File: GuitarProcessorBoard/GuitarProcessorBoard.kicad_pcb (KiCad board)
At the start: 4 copper layers, 141 parts, among them J301 SWD Header, J302 PWR, J303 TAP, J304 MODE, J305 BYP, J306 EXP, J307 ScopeGroundLoop, SW301 RST, SW302 BOOT, SW303 ENC, SW304 BACK, U201 TLV320AIC3204, U202 TL074, U301 STM32H7B0VBT6, U302 TPS63070, U304 74HC595, Y301 32MHz, Y302 32.768kHZ

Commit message: starting layout
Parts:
- removed C208, C213: 100n, Capacitor_SMD:C_0805_2012Metric
- added R220: 22, Resistor_SMD:R_0805_2012Metric, B.Cu at (-134.1, 76.3)
- added R330: 22, Resistor_SMD:R_0805_2012Metric, B.Cu at (-143.9, 74.0)
- added R331: 22, Resistor_SMD:R_0805_2012Metric, B.Cu at (-146.1, 76.3)
- added R332: 22, Resistor_SMD:R_0805_2012Metric, B.Cu at (-141.4, 71.7)
- added R333: 22, Resistor_SMD:R_0805_2012Metric, B.Cu at (-139.9, 70.2)
- C201, C202, C203, C204, C205, C206, C207, C209, C210, C211, C212, C214, C215, C216, C217, C218, C219, C303, C304, C305, C306, C307, C308, C309, C310, C311, C312, C313, C314, C315, C316, C317, C318, C327, C328, C329, C330, C331, C332, C333, C334, D303, D304, FB301, J301, J302, J303, J304, J305, J306, J307, R201, R202, R203, R204, R205, R206, R207, R208, R209, R210, R211, R212, R213, R214, R215, R216, R217, R218, R219, R301, R302, R303, R304, R305, R306, R307, R308, R309, R310, R315, R316, R317, R318, R319, R320, R321, R322, R323, R324, R325, R326, R327, R328, R329, SW301, SW302, TP201, TP202, TP203, TP301, TP302, TP303, U201, U202, U301, U304, Y301, Y302: moved to B.Cu
- C301, C302: value 6p -> 10p; moved to B.Cu
- RV201, RV301, RV302, RV303: footprint Potentiometer_THT:Potentiometer_Alpha_RV16AF_42_Single_Long -> Potentiometer_THT:Potentiometer_Alpha_RD901F-40-00D_Single_Vertical_CircularHoles
- U303: value ~ -> SSD1306_OLED_128x64
- moved SW301 172.5 mm to (-177.6, 83.2), turned to 90 degrees
- moved D307 161.3 mm to (-175.2, 94.0)
- moved U201 156.9 mm to (-124.7, 73.1), turned to 45 degrees
- moved C209 156.4 mm to (-134.2, 54.9)
- moved J305 155.6 mm to (-157.2, 97.5), turned to -90 degrees
- moved C211 153.9 mm to (-130.3, 69.4), turned to -45 degrees
- moved R309 151.9 mm to (-176.1, 87.6), turned to 90 degrees
- moved C210 151.7 mm to (-128.0, 67.0), turned to -45 degrees
- moved C202 151.3 mm to (-129.7, 74.2), turned to 135 degrees
- moved R203 150.0 mm to (-133.4, 62.8), turned to -90 degrees
- moved R202 150.0 mm to (-133.4, 59.0), turned to -90 degrees
- moved D303 149.6 mm to (-172.8, 67.0), turned to -90 degrees
- moved R204 147.6 mm to (-130.9, 57.0), turned to 90 degrees
- moved SW302 147.4 mm to (-159.3, 50.5), turned to 90 degrees
- moved R206 146.6 mm to (-129.9, 62.7), turned to -90 degrees
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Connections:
- R204 pad 2: Net-(U202B--) -> Net-(U202D--)
- R205 pad 1: Net-(U202B--) -> Net-(U202D--)
- R206 pad 2: Net-(U202A--) -> Net-(U202C--)
- R207 pad 1: Net-(U202A--) -> Net-(U202C--)
- R211 pad 2: Net-(U202C--) -> Net-(U202B--)
- R212 pad 1: Net-(U202C--) -> Net-(U202B--)
- R215 pad 2: Net-(U202D--) -> Net-(U202A--)
- R216 pad 2: Net-(U202D--) -> Net-(U202A--)
- R217 pad 1: Net-(U202D--) -> Net-(U202A--)
- R325 pad 2: /MCU/LED_A6 -> /MCU/LED_A5
- U201 pad 5: I2S_SDI -> Net-(U201-DOUT)
- U202 pad 1: /Audio/InputNeg -> Net-(C219-Pad1)
- U202 pad 10: /Audio/Bias2 -> /Audio/Bias1
- U202 pad 12: /Audio/Bias2 -> /Audio/Bias1
- U202 pad 14: Net-(C219-Pad1) -> /Audio/InputPos
- U202 pad 3: /Audio/Bias1 -> /Audio/Bias2
- U202 pad 5: /Audio/Bias1 -> /Audio/Bias2
- U202 pad 7: /Audio/InputPos -> /Audio/Wet
- U202 pad 8: /Audio/Wet -> /Audio/InputNeg
- U301 pad 28: I2S_LR -> Net-(U301-PA4)
- U301 pad 29: I2S_BCLK -> Net-(U301-PA5)
- U301 pad 31: I2S_SDO -> Net-(U301-PA7)
- U301 pad 32: I2S_MCLK -> Net-(U301-PC4)
- U301 pad 45: unconnected-(U301-PE15-Pad45) -> CODEC_NRST
- U304 pad 7: /MCU/LED_A6 -> unconnected-(U304-QH-Pad7)

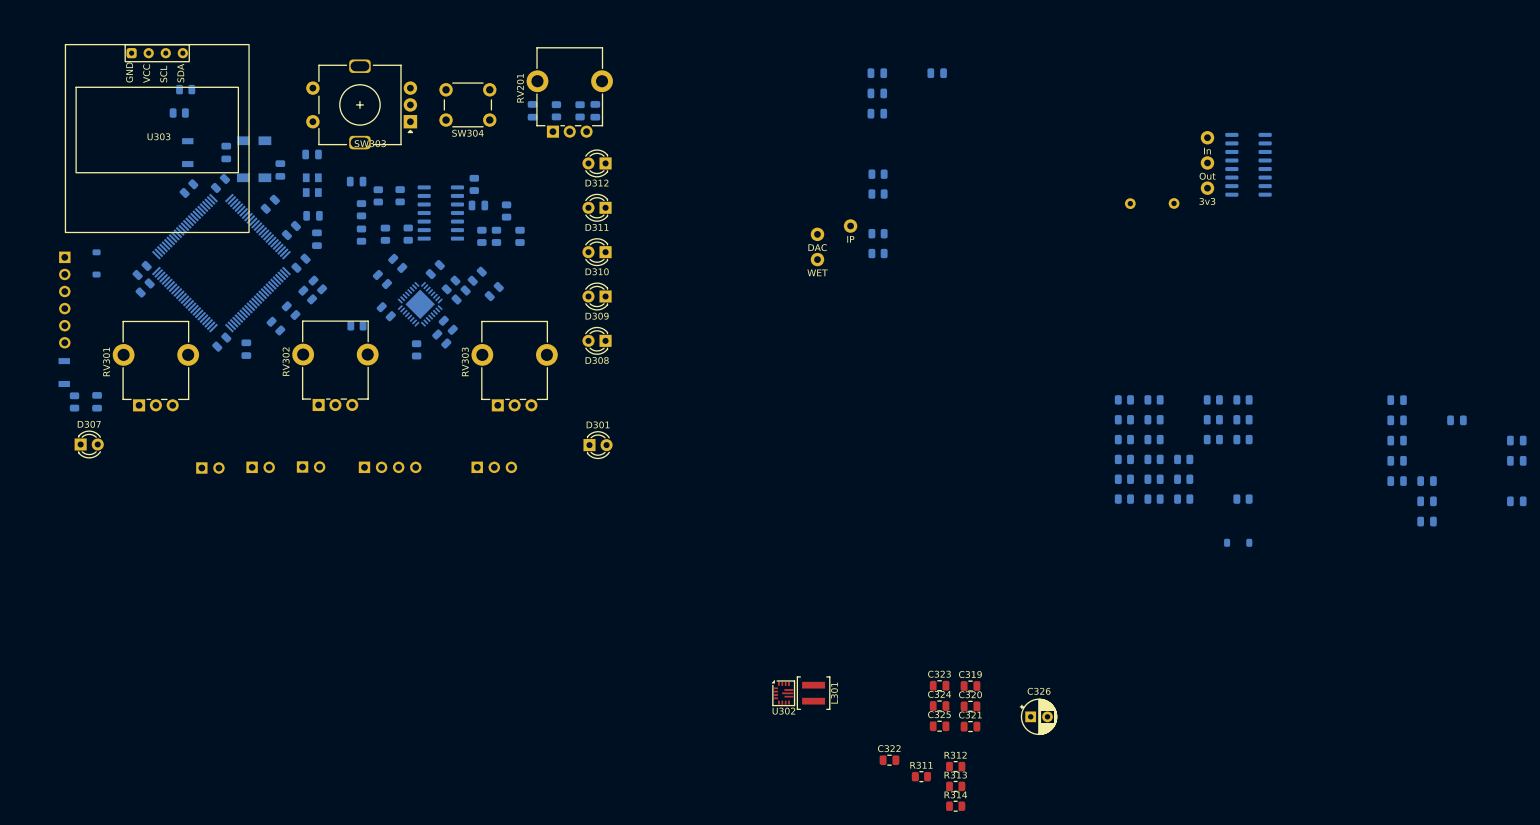
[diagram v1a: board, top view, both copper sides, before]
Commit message: removed encoder and back btn
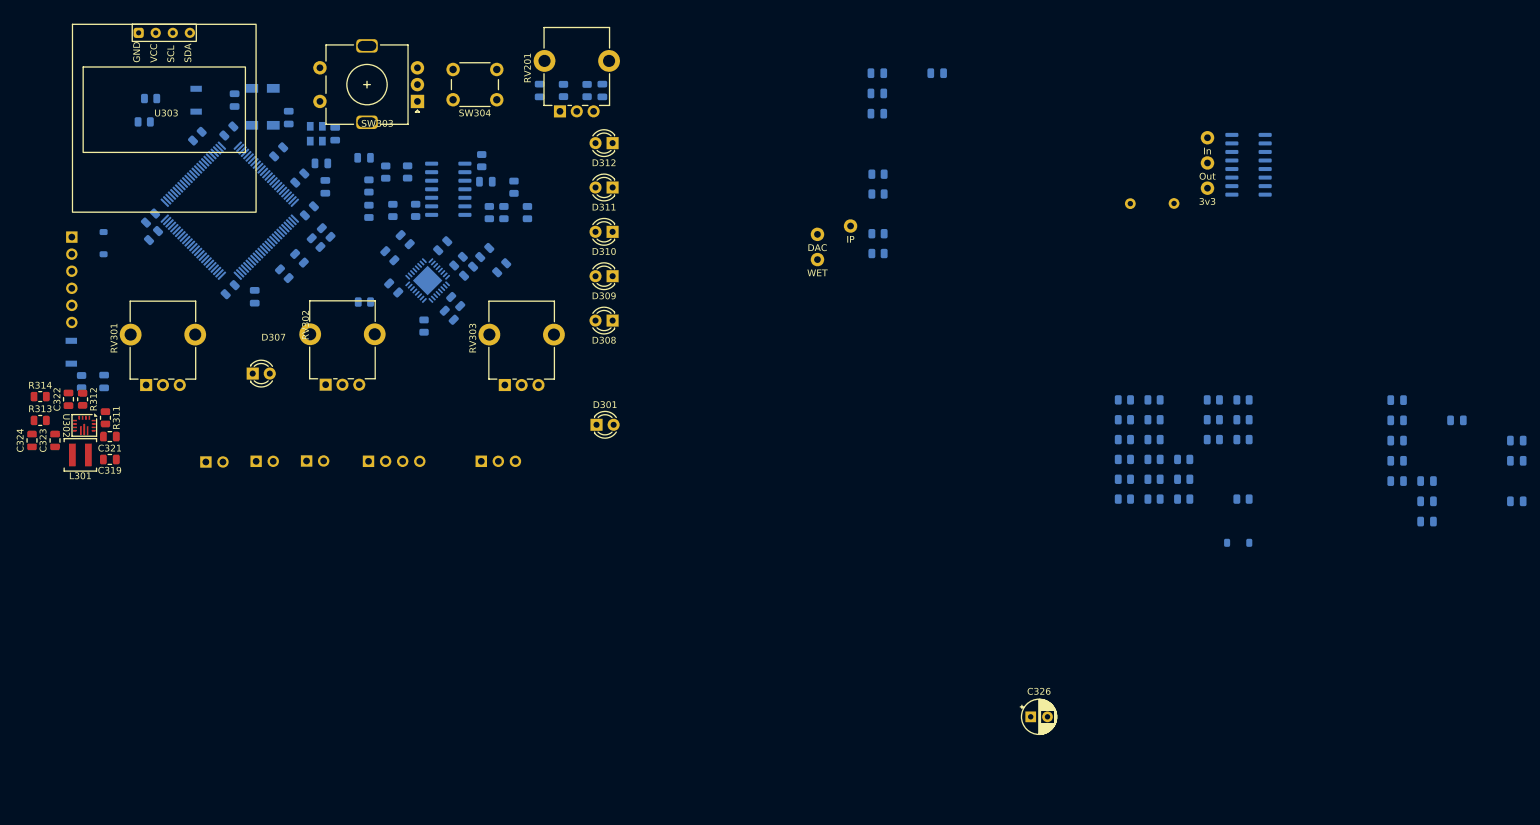
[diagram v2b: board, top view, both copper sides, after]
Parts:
- removed C320: 10u, Capacitor_SMD:C_0805_2012Metric
- removed C325: 22u, Capacitor_SMD:C_0805_2012Metric
- moved R314 149.1 mm to (-181.2, 86.8)
- moved R313 146.6 mm to (-181.2, 90.4)
- moved R312 140.9 mm to (-174.9, 87.2), turned to -90 degrees
- moved C324 140.6 mm to (-182.4, 93.3), turned to -90 degrees
- moved C323 136.5 mm to (-179.0, 93.3), turned to -90 degrees
- moved C321 135.1 mm to (-170.8, 92.8)
- moved C322 133.4 mm to (-177.0, 87.2), turned to 90 degrees
- moved R311 132.6 mm to (-171.5, 90.0), turned to 90 degrees
- moved C319 132.4 mm to (-170.8, 96.2)
- moved L301 114.7 mm to (-175.2, 95.5), turned to 180 degrees
- moved U302 111.4 mm to (-174.6, 91.1), turned to -90 degrees
- moved D307 27.7 mm to (-149.6, 83.4)
- moved C302 7.90 mm to (-139.4, 52.1)
- moved C305 7.90 mm to (-145.7, 50.4)
- moved C307 7.90 mm to (-153.2, 47.3)
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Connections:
- net Net-(U302-FB) renamed /MCU/V_FB

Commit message: first layout
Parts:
- removed C305: 100n, Capacitor_SMD:C_0805_2012Metric
- removed C330, C331: 10n, Capacitor_SMD:C_0805_2012Metric
- removed R319, R320: 47k, Resistor_SMD:R_0805_2012Metric
- removed R321: 100k, Resistor_SMD:R_0805_2012Metric
- removed SW303: ENC, Rotary_Encoder:RotaryEncoder_Alps_EC11E-Switch_Vertical_H20mm_5Pin
- removed SW304: BACK, Button_Switch_THT:SW_PUSH_6mm
- removed TP201: IP, TestPoint:TestPoint_THTPad_D2.0mm_Drill1.0mm_VAL
- added D302: ORANGE, LED_THT:LED_D3.0mm, F.Cu at (-95.8, 83.2)
- C304, C306, C333, R305, R306, R307, R308, R322, R323, R324, R325, U304: moved to F.Cu
- C326: moved to B.Cu
- R318: value 100k -> 470; moved to F.Cu
- moved C304 216.2 mm to (-172.7, 49.5), turned to 90 degrees
- moved C306 199.8 mm to (-156.0, 56.3), turned to -135 degrees
- moved C327 192.0 mm to (-166.2, 82.8), turned to 90 degrees
- moved C316 169.9 mm to (-137.4, 58.5)
- moved TP303 169.0 mm to (-176.6, 52.7)
- moved C332 167.4 mm to (-137.8, 39.0), turned to 0 degrees
- moved C328 165.6 mm to (-139.4, 82.8), turned to 90 degrees
- moved C303 162.8 mm to (-123.8, 79.0), turned to 0 degrees
- moved C326 160.1 mm to (-169.8, 49.9)
- moved R307 155.7 mm to (-152.4, 35.2), turned to 0 degrees
- moved R315 152.3 mm to (-162.9, 82.8), turned to 90 degrees
- moved C329 142.4 mm to (-115.6, 83.1), turned to 90 degrees
- moved C334 142.0 mm to (-120.8, 86.8), turned to 0 degrees
- moved FB301 137.5 mm to (-137.4, 62.0)
- moved J307 136.5 mm to (-150.7, 80.3)
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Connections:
- R318 pad 1: +3.3V -> Net-(D302-A)
- R318 pad 2: ENC_B -> /MCU/LED_A6
- U301 pad 51: ENC_B -> unconnected-(U301-PB12-Pad51)
- U301 pad 52: ENC_R -> unconnected-(U301-PB13-Pad52)
- U301 pad 53: ENC_L -> unconnected-(U301-PB14-Pad53)
- U301 pad 67: BACK_BTN -> unconnected-(U301-PA8-Pad67)
- U304 pad 1: /MCU/LED_BYPASS -> /MCU/LED_A5
- U304 pad 15: /MCU/LED_TEMPO -> /MCU/LED_A6
- U304 pad 2: /MCU/LED_A1 -> /MCU/LED_A4
- U304 pad 3: /MCU/LED_A2 -> /MCU/LED_A3
- U304 pad 4: /MCU/LED_A3 -> /MCU/LED_A2
- U304 pad 5: /MCU/LED_A4 -> /MCU/LED_A1
- U304 pad 6: /MCU/LED_A5 -> /MCU/LED_TEMPO
- U304 pad 7: unconnected-(U304-QH-Pad7) -> /MCU/LED_BYPASS
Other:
- board text added: "GND"
- board text added: "NRST"
- board text added: "SWCLK"
- board text added: "SWDIO"
- board text added: "SWO"
- board text added: "VCC"

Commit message: routing rd one
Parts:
- moved J303 15.0 mm to (-157.1, 92.9)
- moved J305 14.9 mm to (-142.2, 92.8)
- moved R328 9.56 mm to (-145.1, 86.3)
- moved C315 9.34 mm to (-147.8, 45.8)
- moved R326 9.23 mm to (-153.9, 86.3)
- moved C317 7.02 mm to (-155.7, 44.8)
- moved C302 6.19 mm to (-148.7, 53.8), turned to 135 degrees
- moved C301 4.01 mm to (-143.6, 52.6), turned to 45 degrees
- moved C209 3.66 mm to (-129.4, 45.7), turned to 180 degrees
- moved Y301 2.31 mm to (-145.6, 50.6), turned to -135 degrees
- moved C304 1.76 mm to (-173.8, 50.9), turned to -90 degrees
- moved C311 1.54 mm to (-156.2, 73.2)
- moved C205 1.50 mm to (-122.0, 75.9)
- moved R322 1.23 mm to (-100.6, 57.1), turned to -90 degrees
- moved R323 1.20 mm to (-100.6, 63.8), turned to -90 degrees
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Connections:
- Y302 pad 1: LFE_IN -> LFE_OUT
- Y302 pad 4: LFE_OUT -> LFE_IN
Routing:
- net +3.3V: track 0.00 -> 287.8 mm, vias 0 -> 11
- net VCC: track 0.00 -> 124.9 mm, vias 0 -> 2
- net GND: track 0.00 -> 82.8 mm, vias 0 -> 60
- net NRST: track 0.00 -> 73.8 mm, vias 0 -> 2
- net +9V: track 0.00 -> 73.7 mm
- net /MCU/LED_BYPASS: track 0.00 -> 71.9 mm
- net /MCU/LED_TEMPO: track 0.00 -> 51.9 mm
- net FX_IN: track 0.00 -> 51.9 mm
- net ADC_A: track 0.00 -> 45.4 mm, vias 0 -> 2
- net BYP_BTN: track 0.00 -> 41.2 mm
- net MODE_BTN: track 0.00 -> 38.2 mm
- net TAP_BTN: track 0.00 -> 35.8 mm
- net SWO: track 0.00 -> 35.7 mm
- net CODEC_NRST: track 0.00 -> 33.7 mm
- net CODEC_SDA: track 0.00 -> 31.6 mm, vias 0 -> 2
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- added copper zone on In1.Cu, net GND
- added copper zone on In2.Cu, net GND

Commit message: routed & DRC passing
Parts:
- moved J307 46.0 mm to (-110.5, 58.0)
- moved TP302 22.8 mm to (-103.6, 87.5)
- moved C207 4.51 mm to (-99.8, 37.4), turned to -90 degrees
- moved TP301 2.44 mm to (-129.6, 85.8)
- moved R201 1.05 mm to (-125.8, 76.5)
- moved J301 0.65 mm to (-175.8, 63.1)
- turned TP202 to -45 degrees
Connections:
- U301 pad 1: LED_SCK -> unconnected-(U301-PE2-Pad1)
- U301 pad 3: LED_LATCH -> unconnected-(U301-PE4-Pad3)
- U301 pad 4: LED_NRST -> unconnected-(U301-PE5-Pad4)
- U301 pad 5: LED_DATA -> unconnected-(U301-PE6-Pad5)
- U301 pad 51: unconnected-(U301-PB12-Pad51) -> LED_LATCH
- U301 pad 52: unconnected-(U301-PB13-Pad52) -> LED_SCK
- U301 pad 53: unconnected-(U301-PB14-Pad53) -> LED_NRST
- U301 pad 54: unconnected-(U301-PB15-Pad54) -> LED_DATA
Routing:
- net FX_IN: track 51.9 -> 134.8 mm, vias 0 -> 1
- net ADC_C: track 3.99 -> 85.4 mm, vias 0 -> 2
- net LED_DATA: track 0.00 -> 75.0 mm, vias 0 -> 1
- net +3.3V: track 287.8 -> 362.8 mm, vias 11 -> 14
- net LED_LATCH: track 0.00 -> 73.8 mm, vias 0 -> 1
- net FX_OUT: track 23.1 -> 95.9 mm, vias 0 -> 3
- net LED_SCK: track 0.00 -> 71.2 mm, vias 0 -> 1
- net LED_NRST: track 3.68 -> 69.4 mm, vias 0 -> 1
- net ADC_EXP: track 3.34 -> 69.0 mm, vias 0 -> 4
- net ADC_B: track 4.00 -> 60.9 mm, vias 0 -> 2
- net DISP_SDA: track 7.42 -> 53.5 mm, vias 0 -> 2
- net DISP_SCL: track 10.9 -> 53.4 mm, vias 0 -> 2
- net /MCU/LED_TEMPO: track 51.9 -> 32.7 mm
- net SWO: track 35.7 -> 26.3 mm, vias 0 -> 1
- net +9V: track 73.7 -> 82.1 mm, vias 0 -> 3
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- added copper zone on B.Cu, net GND
- added copper zone on F.Cu, net GND
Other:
- board outline added: 86 x 65 mm

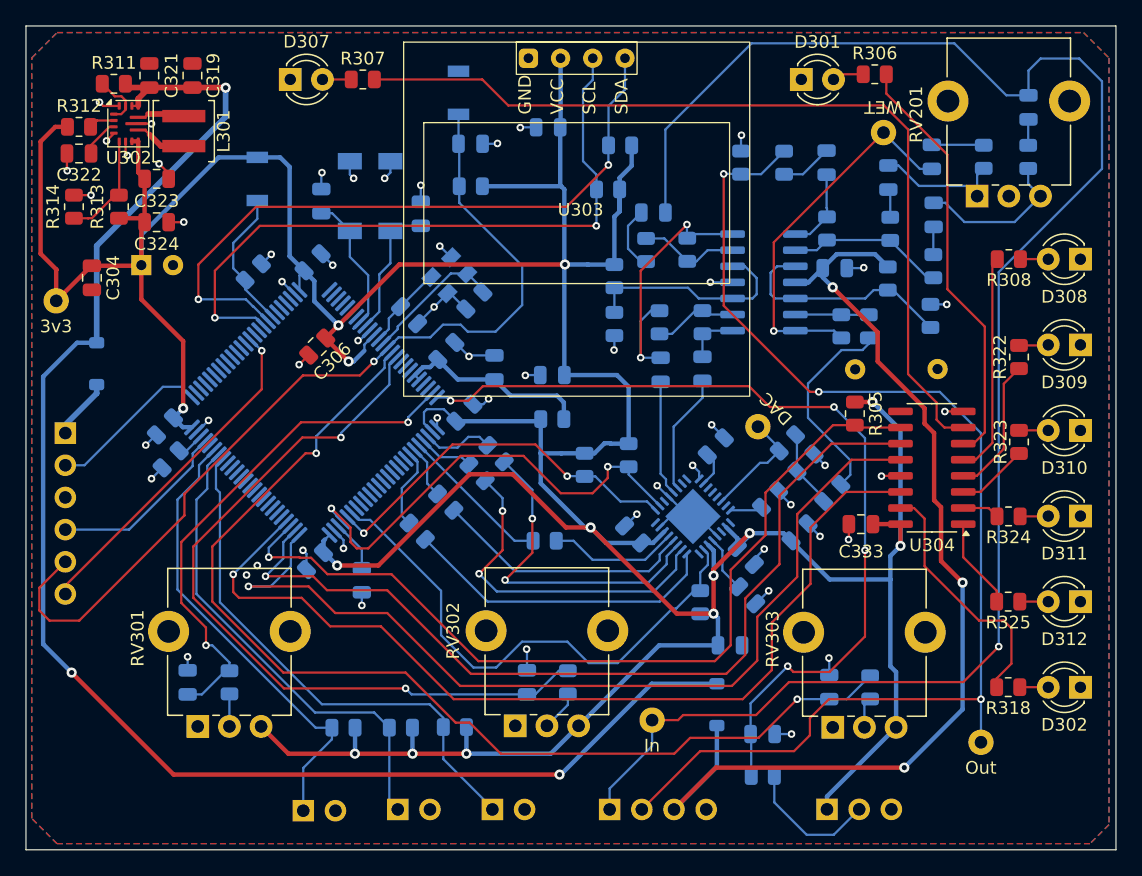
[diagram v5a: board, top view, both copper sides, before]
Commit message: silkscreen, stitching vias
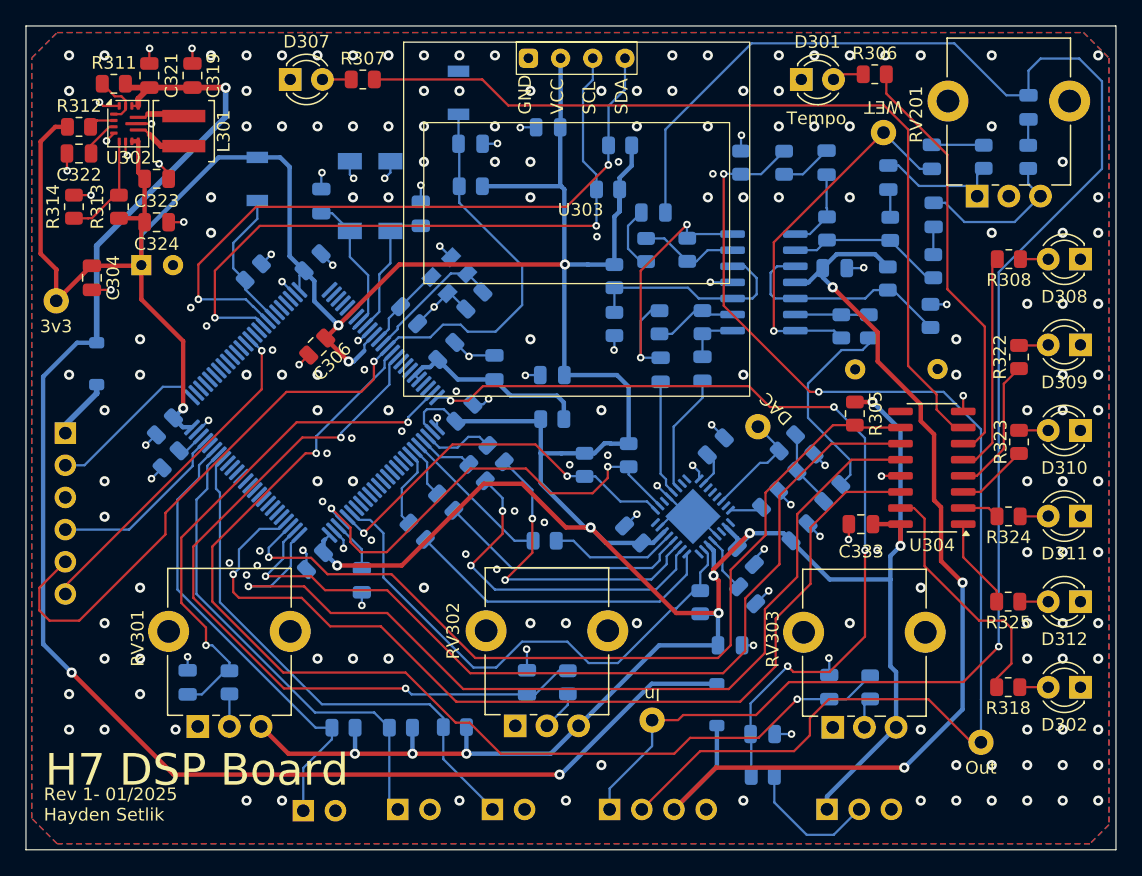
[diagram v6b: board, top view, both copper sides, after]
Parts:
- turned TP301 to 0 degrees
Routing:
- net GND: track 79.2 -> 83.8 mm, vias 54 -> 217
- net FX_OUT: track 95.9 -> 97.5 mm, vias 3 -> 2
- net LED_DATA: track 75.0 -> 76.1 mm
- net NRST: track 71.9 -> 72.8 mm
- net CODEC_SDA: track 36.6 -> 36.0 mm
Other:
- board text added: "+9V"
- board text added: "3v3"
- board text added: "ALG"
- board text added: "BYP"
- board text added: "EXP"
- board text added: "H7 DSP Board"
- board text added: "IN"
- board text added: "OUT"
- board text added: "Rev 1- 01/2025 Hayden Setlik"
- board text added: "TAP"
- board text added: "Tempo"

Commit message: more test points, trace clean up
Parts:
- added TP304: VCC, TestPoint:TestPoint_THTPad_D2.0mm_Drill1.0mm_VAL, F.Cu at (-170.0, 56.0)
- added TP305: FB, TestPoint:TestPoint_THTPad_D2.0mm_Drill1.0mm_VAL, F.Cu at (-175.9, 48.4)
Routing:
- net VCC: track 121.5 -> 124.9 mm
- net /MCU/V_FB: track 8.21 -> 10.7 mm
- net GND: vias 217 -> 216
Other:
- board text added: "Bypass"

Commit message: rev1 gerber
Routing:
- net GND: track 83.8 -> 85.7 mm, vias 216 -> 204
- net +3.3V: track 363.0 -> 363.5 mm
